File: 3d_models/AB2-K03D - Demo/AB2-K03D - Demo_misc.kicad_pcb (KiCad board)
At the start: 2 copper layers, 38 parts

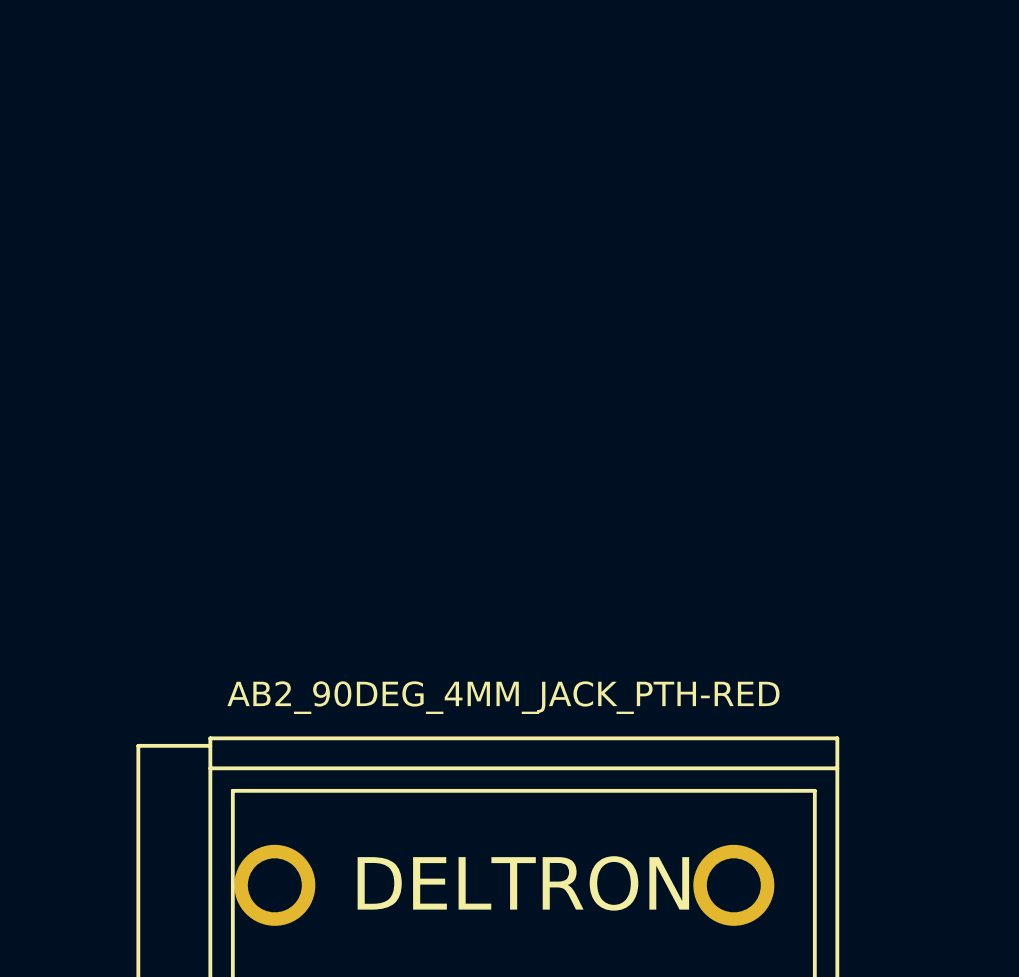
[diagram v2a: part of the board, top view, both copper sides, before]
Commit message: 3d: AB2-K03D: misc: add blu yel 90' 4mm banana jacks
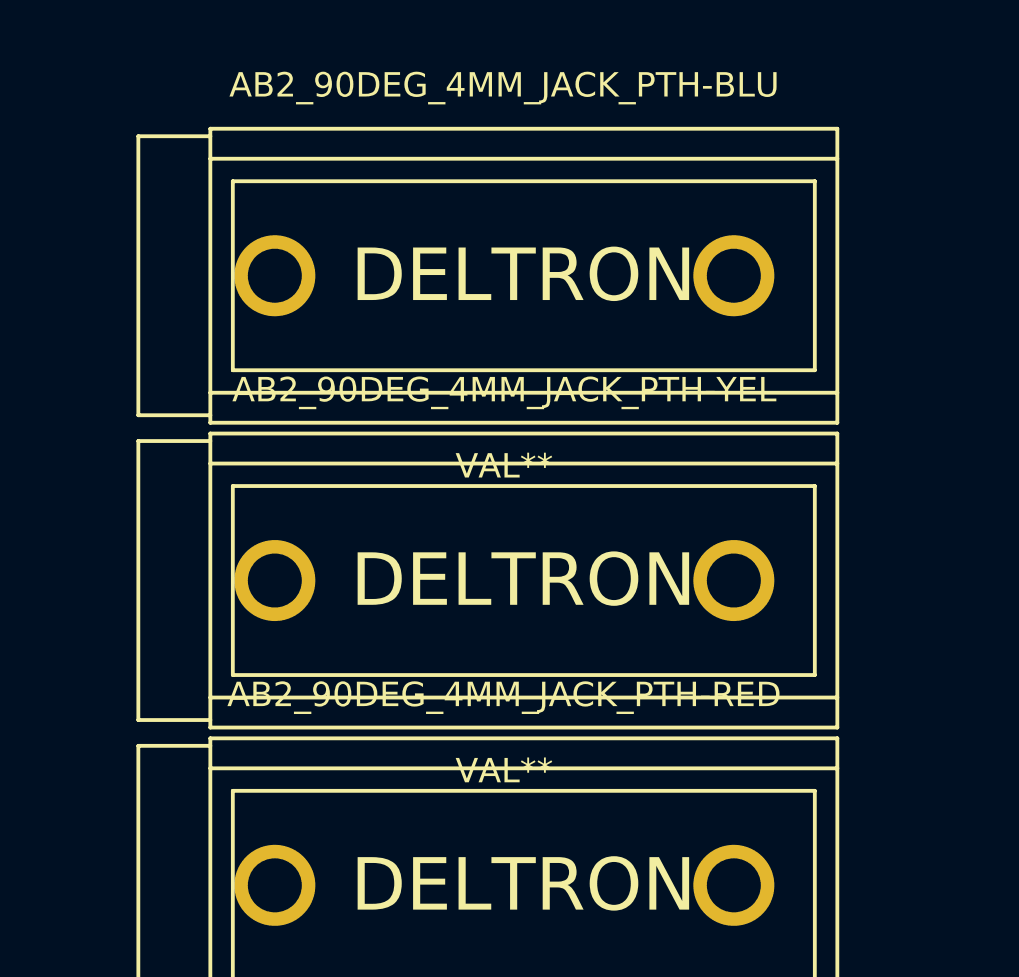
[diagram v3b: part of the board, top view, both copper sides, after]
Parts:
- added AB2_90DEG_4MM_JACK_PTH-BLU: VAL**, AB2_90DEG_4MM_JACK_PTH-BLU, F.Cu at (21.6, 162.6)
- added AB2_90DEG_4MM_JACK_PTH-YEL: VAL**, AB2_90DEG_4MM_JACK_PTH-YEL, F.Cu at (21.6, 172.7)
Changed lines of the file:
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@@
     (links 0)
     (no_connects 0)
-    (area 6.9215 201.333258 233.997501 286.4485)
+    (area 6.9215 175.8315 233.997501 286.4485)
     (thickness 1.6)
     (drawings 0)
     (tracks 0)
     (zones 0)
-    (modules 38)
+    (modules 40)
     (nets 1)
   )
@@
       (at (xyz 0 0 0))
       (scale (xyz 0.3937 0.3937 0.3937))
+      (rotate (xyz 0 0 180))
+    )
+  )
+  (module AB2_90DEG_4MM_JACK_PTH-YEL (layer F.Cu)
+    (at 21.59 172.72)
+    (fp_text reference AB2_90DEG_4MM_JACK_PTH-YEL (at 0 -6.35) (layer F.SilkS)
+      (effects (font (size 0.8128 0.8128) (thickness 0.0762)))
+    )
+    (fp_text value VAL** (at 0 6.35) (layer F.SilkS)
+      (effects (font (size 0.8128 0.8128) (thickness 0.0762)))
+    )
+    (fp_line (start -9.05 -3.15) (end 10.35 -3.15) (layer F.SilkS) (width 0.127))
+    (fp_line (start 10.35 -3.15) (end 10.35 3.15) (layer F.SilkS) (width 0.127))
+    (fp_line (start 10.35 3.15) (end -9.05 3.15) (layer F.SilkS) (width 0.127))
+    (fp_line (start -9.05 3.15) (end -9.05 -3.15) (layer F.SilkS) (width 0.127))
+    (fp_line (start -9.8 3.9) (end 11.1 3.9) (layer F.SilkS) (width 0.127))
+    (fp_line (start -9.8 -3.9) (end 11.1 -3.9) (layer F.SilkS) (width 0.127))
+    (fp_text user DELTRON (at 0.635 0) (layer F.SilkS)
+      (effects (font (size 1.75 1.75) (thickness 0.2)))
+    )
+    (fp_line (start -9.8 -4.65) (end -12.2 -4.65) (layer F.SilkS) (width 0.127))
+    (fp_line (start -12.2 -4.65) (end -12.2 4.65) (layer F.SilkS) (width 0.127))
+    (fp_line (start -12.2 4.65) (end -9.8 4.65) (layer F.SilkS) (width 0.127))
+    (fp_line (start -9.8 -4.9) (end -9.8 4.9) (layer F.SilkS) (width 0.127))
+    (fp_line (start -9.8 4.9) (end 11.1 4.9) (layer F.SilkS) (width 0.127))
+    (fp_line (start 11.1 4.9) (end 11.1 -4.9) (layer F.SilkS) (width 0.127))
+    (fp_line (start 11.1 -4.9) (end -9.8 -4.9) (layer F.SilkS) (width 0.127))
+    (pad 1 thru_hole circle (at -7.65 0) (size 2.7 2.7) (drill 1.8)
+      (layers *.Cu *.Mask F.SilkS)
+    )
+    (pad 1 thru_hole circle (at 7.65 0) (size 2.7 2.7) (drill 1.8)
+      (layers *.Cu *.Mask F.SilkS)
+    )
+    (model ../3d_models/ab2_power/AB2_90DEG_4MM_JACK_PTH-YEL.wrl
+      (at (xyz 0 0 0))
+      (scale (xyz 0.3937 0.3937 0.3937))
+      (rotate (xyz 0 0 180))
+    )
+  )
+  (module AB2_90DEG_4MM_JACK_PTH-BLU (layer F.Cu)
+    (at 21.59 162.56)
+    (fp_text reference AB2_90DEG_4MM_JACK_PTH-BLU (at 0 -6.35) (layer F.SilkS)
+      (effects (font (size 0.8128 0.8128) (thickness 0.0762)))
+    )
+    (fp_text value VAL** (at 0 6.35) (layer F.SilkS)
+      (effects (font (size 0.8128 0.8128) (thickness 0.0762)))
+    )
+    (fp_line (start -9.05 -3.15) (end 10.35 -3.15) (layer F.SilkS) (width 0.127))
+    (fp_line (start 10.35 -3.15) (end 10.35 3.15) (layer F.SilkS) (width 0.127))
+    (fp_line (start 10.35 3.15) (end -9.05 3.15) (layer F.SilkS) (width 0.127))
+    (fp_line (start -9.05 3.15) (end -9.05 -3.15) (layer F.SilkS) (width 0.127))
+    (fp_line (start -9.8 3.9) (end 11.1 3.9) (layer F.SilkS) (width 0.127))
+    (fp_line (start -9.8 -3.9) (end 11.1 -3.9) (layer F.SilkS) (width 0.127))
+    (fp_text user DELTRON (at 0.635 0) (layer F.SilkS)
+      (effects (font (size 1.75 1.75) (thickness 0.2)))
+    )
+    (fp_line (start -9.8 -4.65) (end -12.2 -4.65) (layer F.SilkS) (width 0.127))
+    (fp_line (start -12.2 -4.65) (end -12.2 4.65) (layer F.SilkS) (width 0.127))
+    (fp_line (start -12.2 4.65) (end -9.8 4.65) (layer F.SilkS) (width 0.127))
+    (fp_line (start -9.8 -4.9) (end -9.8 4.9) (layer F.SilkS) (width 0.127))
+    (fp_line (start -9.8 4.9) (end 11.1 4.9) (layer F.SilkS) (width 0.127))
+    (fp_line (start 11.1 4.9) (end 11.1 -4.9) (layer F.SilkS) (width 0.127))
+    (fp_line (start 11.1 -4.9) (end -9.8 -4.9) (layer F.SilkS) (width 0.127))
+    (pad 1 thru_hole circle (at -7.65 0) (size 2.7 2.7) (drill 1.8)
+      (layers *.Cu *.Mask F.SilkS)
+    )
+    (pad 1 thru_hole circle (at 7.65 0) (size 2.7 2.7) (drill 1.8)
+      (layers *.Cu *.Mask F.SilkS)
+    )
+    (model ../3d_models/ab2_power/AB2_90DEG_4MM_JACK_PTH-BLU.wrl
+      (at (xyz 0 0 0))
+      (scale (xyz 0.3937 0.3937 0.3937))
